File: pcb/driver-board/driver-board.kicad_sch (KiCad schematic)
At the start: 24 parts, among them Q3 IRLML6344, Q4 IRLML6344, Q5 IRLML6344

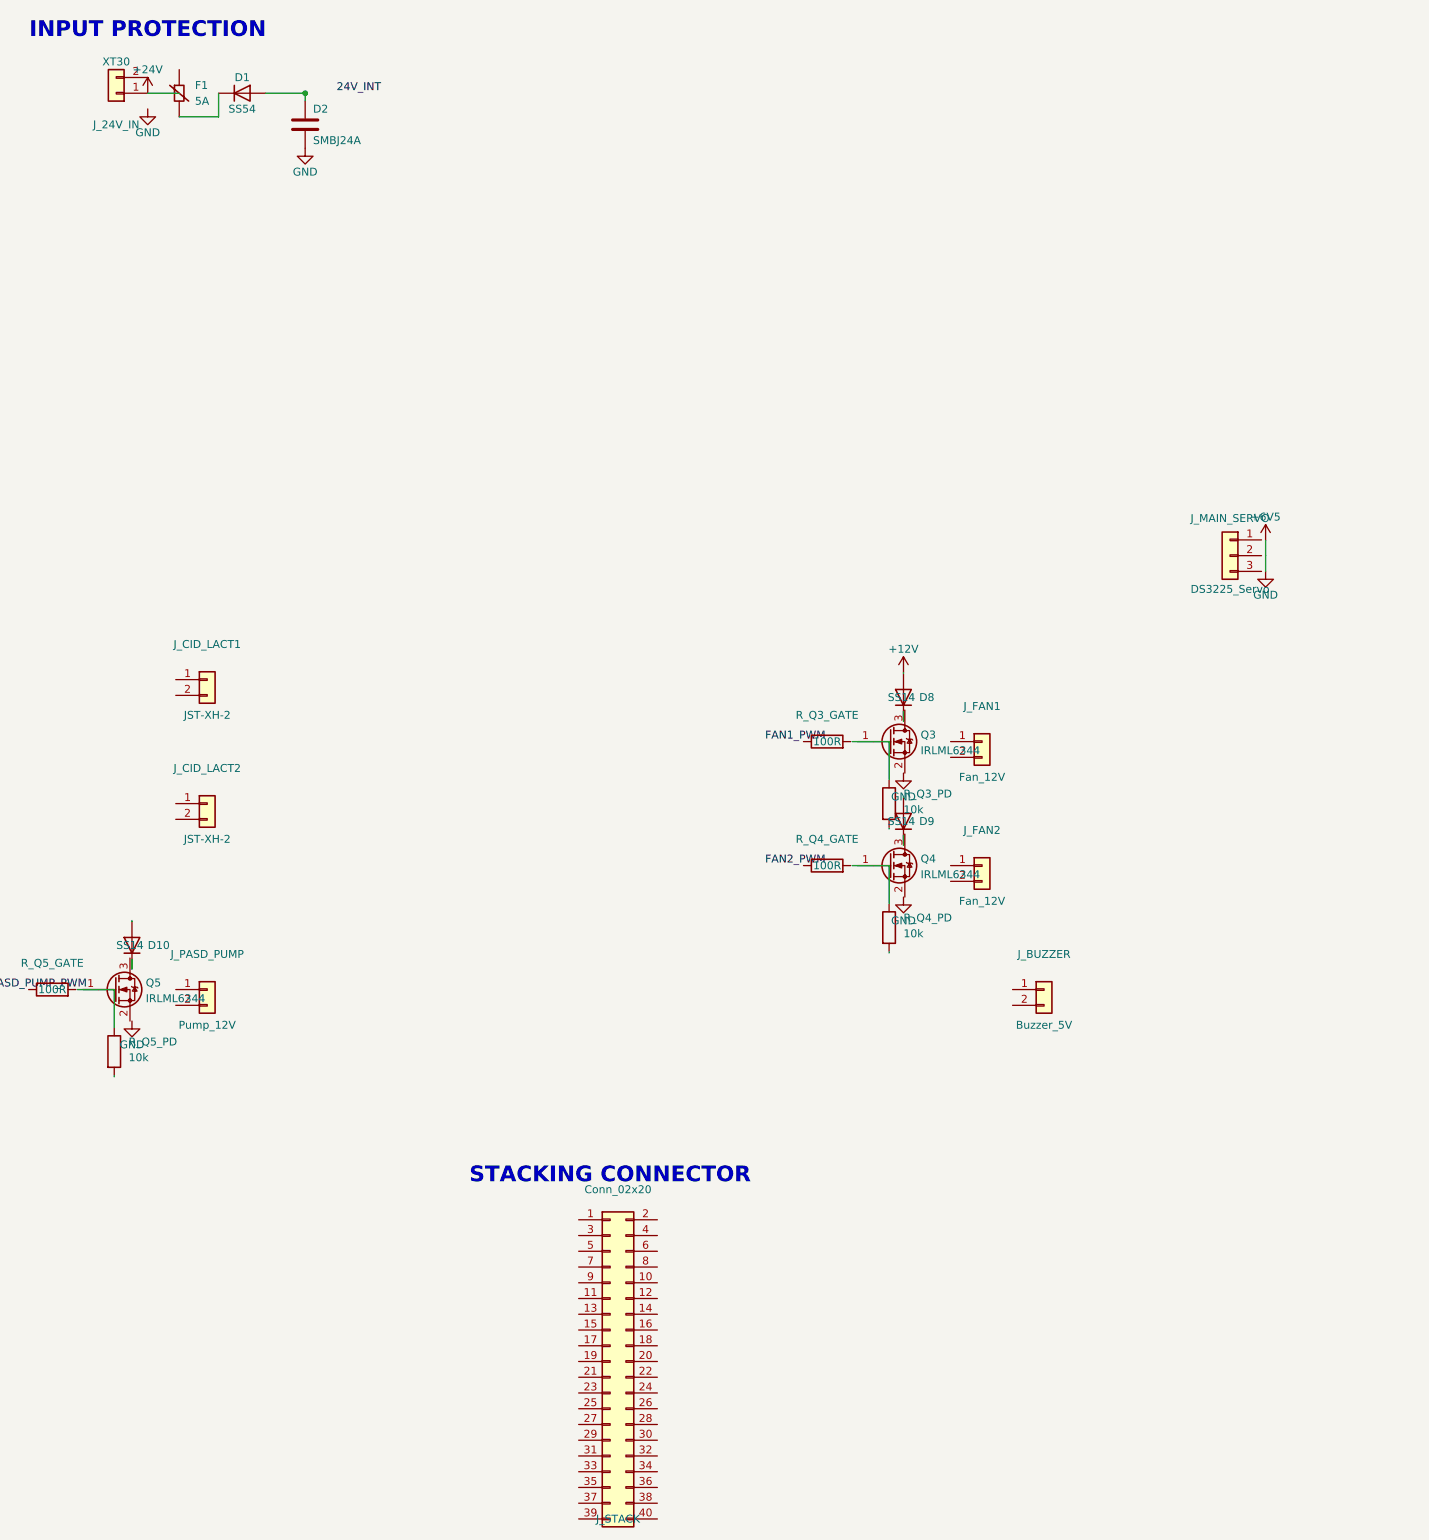
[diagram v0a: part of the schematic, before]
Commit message: Add driver board KiCAD PCB files, update to KiCAD 9, CM5IO off-the-shelf
- Create driver-board KiCAD 9 project: schematic, PCB layout, lib tables
- Update all PCB files from KiCAD 8 to KiCAD 9.0 (generator version,
  KICAD8_*_DIR → KICAD9_*_DIR env vars)
- Fix controller schematic parenthesis syntax error (pin 27/28)
- Update CM5IO Board status to off-the-shelf across all docs
  (was "Custom design required")
- Update docs: Repository Plan, Architecture, Components, Resource
  Allocation, PCB epic

Co-Authored-By: Claude Opus 4.6 <noreply@anthropic.com>
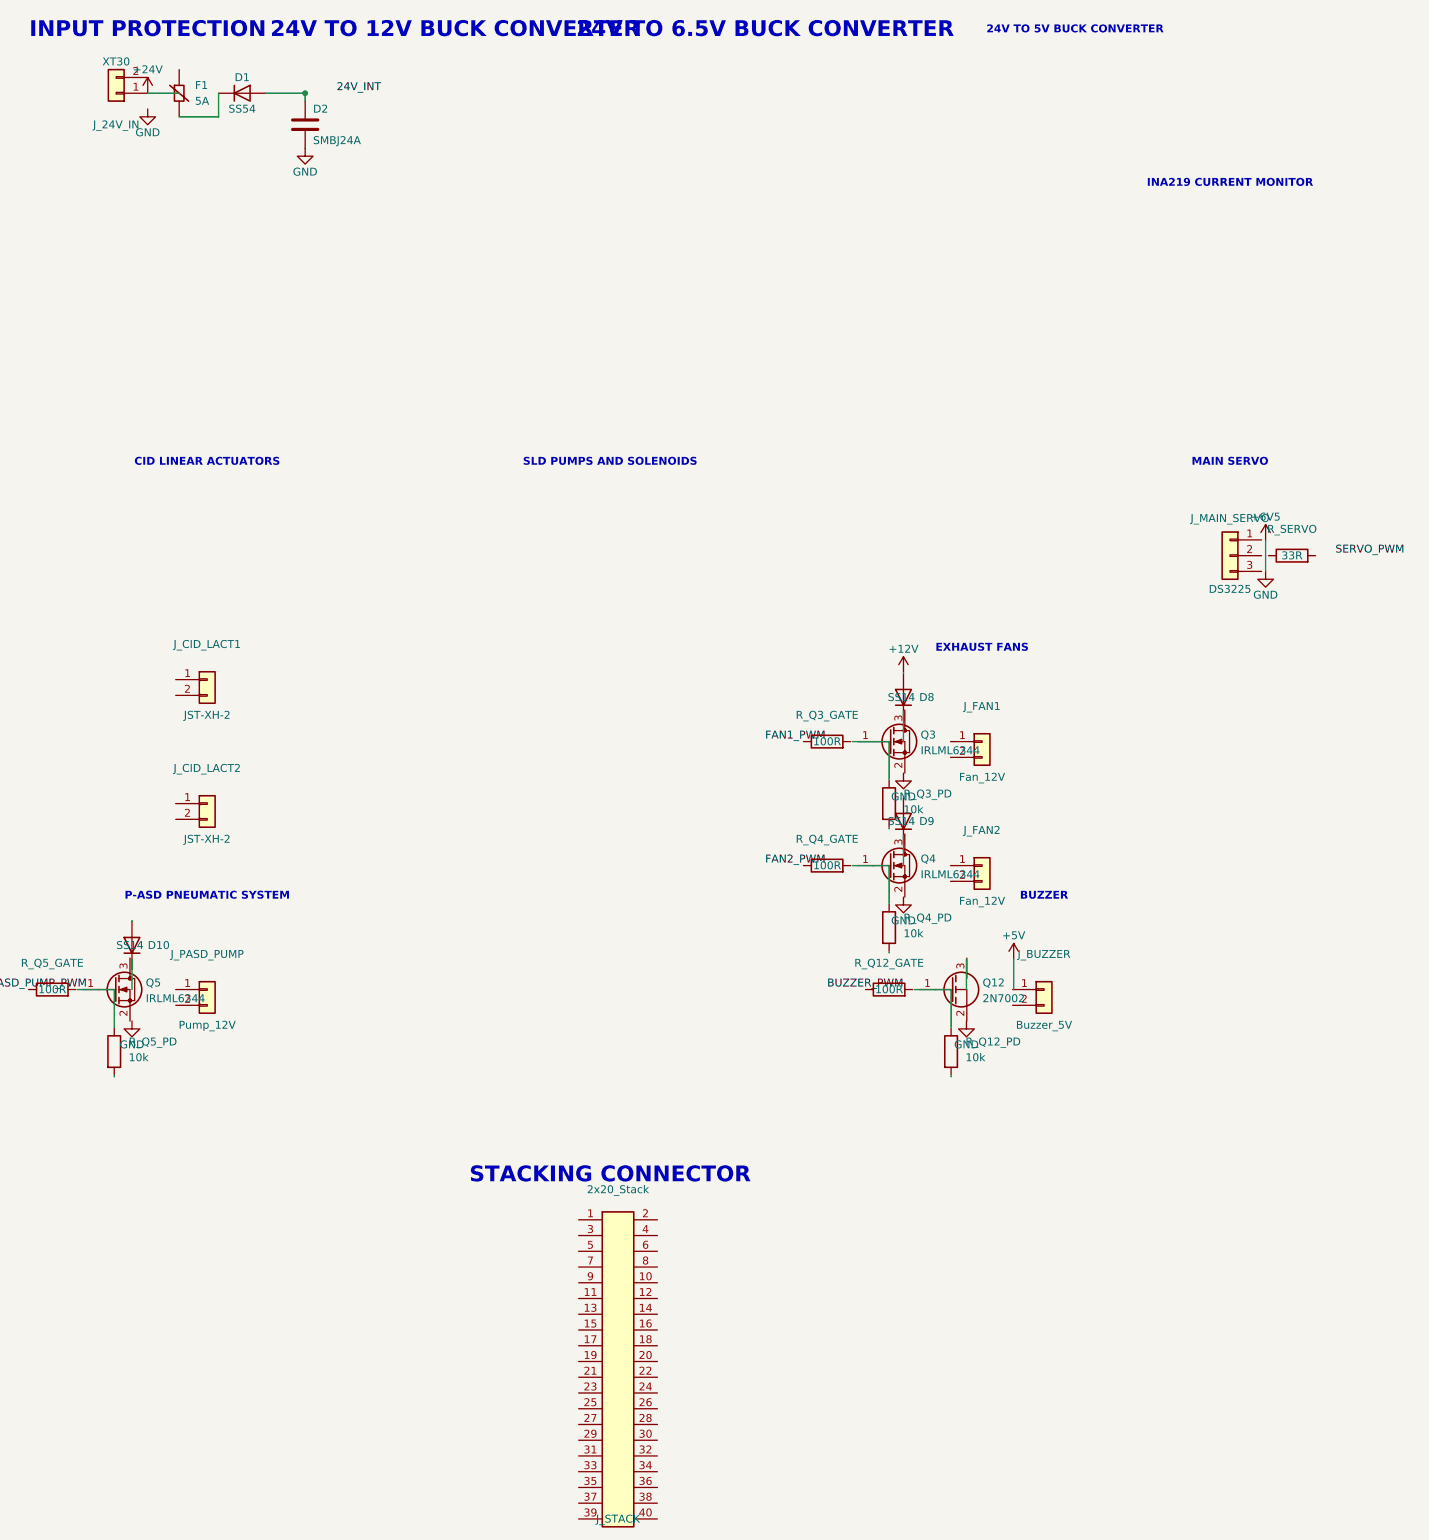
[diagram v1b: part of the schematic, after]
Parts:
- added Q12: 2N7002, Package_TO_SOT_SMD:SOT-23, symbol Transistor_FET:2N7002
- added R_Q12_GATE: 100R, Resistor_SMD:R_0603_1608Metric, symbol Device:R
- added R_Q12_PD: 10k, Resistor_SMD:R_0603_1608Metric, symbol Device:R
- added R_SERVO: 33R, Resistor_SMD:R_0603_1608Metric, symbol Device:R
- J_MAIN_SERVO: value DS3225_Servo -> DS3225
- J_STACK: value Conn_02x20 -> 2x20_Stack
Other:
- note added: "24V TO 12V BUCK CONVERTER"
- note added: "24V TO 5V BUCK CONVERTER"
- note added: "24V TO 6.5V BUCK CONVERTER"
- note added: "BUZZER"
- note added: "CID LINEAR ACTUATORS"
- note added: "EXHAUST FANS"
- note added: "INA219 CURRENT MONITOR"
- note added: "MAIN SERVO"
- note added: "P-ASD PNEUMATIC SYSTEM"
- note added: "SLD PUMPS AND SOLENOIDS"

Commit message: Fix driver board KiCad file syntax errors and update design files
Fix S-expression parsing errors: remove extra generator arg, convert bare
bold keyword to (bold yes), remove invalid (justify center) clauses.

Co-Authored-By: Claude Opus 4.6 <noreply@anthropic.com>
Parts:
- added C_BULK1: 470uF/10V, Capacitor_THT:CP_Radial_D8.0mm_P3.50mm, symbol Device:C_Polarized
- added C_BULK3: 100uF/25V, Capacitor_THT:CP_Radial_D6.3mm_P2.50mm, symbol Device:C_Polarized
- added C_BULK5V: 220uF/10V, Capacitor_THT:CP_Radial_D6.3mm_P2.50mm, symbol Device:C_Polarized
- added C_IN1, C_IN2, C_IN3: 10uF, Capacitor_SMD:C_0805_2012Metric, symbol Device:C
- added C_OUT1a, C_OUT1b, C_OUT2a, C_OUT2b, C_OUT3a, C_OUT3b: 22uF, Capacitor_SMD:C_0805_2012Metric, symbol Device:C
- added C_VCC6, C_VDD8, C_VM4, C_VM5, C_VM6, C_VS7: 100nF, Capacitor_SMD:C_0402_1005Metric, symbol Device:C
- added D11, D12, D13, D14, D15, D16, D6, D7: SS14, Diode_SMD:D_SMA, symbol Diode:SS54
- added D3: SMBJ12A, Diode_SMD:D_SMB, symbol Device:C
- added D4: SMBJ6.5A, Diode_SMD:D_SMB, symbol Device:C
- added D5: SMBJ5.0A, Diode_SMD:D_SMB, symbol Device:C
- added D_BST1, D_BST2, D_BST3: SS34, Diode_SMD:D_SMA, symbol Diode:SS54
- added F2: 1.5A, Resistor_SMD:R_0805_2012Metric, symbol Device:Polyfuse
- added F3: 3A, Resistor_SMD:R_1206_3216Metric, symbol Device:Polyfuse
- added F4: 2A, Resistor_SMD:R_1206_3216Metric, symbol Device:Polyfuse
- added J_PASD_SOL1: PASD_SOL1, Connector_JST:JST_XH_B2B-XH-A_1x02_P2.50mm_Vertical, symbol Connector_Generic:Conn_01x02
- added J_PASD_SOL2: PASD_SOL2, Connector_JST:JST_XH_B2B-XH-A_1x02_P2.50mm_Vertical, symbol Connector_Generic:Conn_01x02
- added J_PASD_SOL3: PASD_SOL3, Connector_JST:JST_XH_B2B-XH-A_1x02_P2.50mm_Vertical, symbol Connector_Generic:Conn_01x02
- added J_PASD_SOL4: PASD_SOL4, Connector_JST:JST_XH_B2B-XH-A_1x02_P2.50mm_Vertical, symbol Connector_Generic:Conn_01x02
- added J_PASD_SOL5: PASD_SOL5, Connector_JST:JST_XH_B2B-XH-A_1x02_P2.50mm_Vertical, symbol Connector_Generic:Conn_01x02
- added J_PASD_SOL6: PASD_SOL6, Connector_JST:JST_XH_B2B-XH-A_1x02_P2.50mm_Vertical, symbol Connector_Generic:Conn_01x02
- added J_SLD: SLD, Connector_JST:JST_XH_B8B-XH-A_1x08_P2.50mm_Vertical, symbol Connector_Generic:Conn_01x08
- added J_SLD_SOL1: SLD_SOL1, Connector_JST:JST_XH_B2B-XH-A_1x02_P2.50mm_Vertical, symbol Connector_Generic:Conn_01x02
- added J_SLD_SOL2: SLD_SOL2, Connector_JST:JST_XH_B2B-XH-A_1x02_P2.50mm_Vertical, symbol Connector_Generic:Conn_01x02
- added L1: 33uH, Inductor_SMD:L_1210_3225Metric, symbol Device:L
- added L2, L3: 22uH, Inductor_SMD:L_1210_3225Metric, symbol Device:L
- added Q1, Q10, Q11, Q2, Q6, Q7, Q8, Q9: IRLML6344, Package_TO_SOT_SMD:SOT-23, symbol Transistor_FET:IRLML6344
- added R_FB1_BOT, R_FB2_BOT, R_FB3_BOT, R_Q10_PD, R_Q11_PD, R_Q1_PD, R_Q2_PD, R_Q6_PD, R_Q7_PD, R_Q8_PD, R_Q9_PD: 10k, Resistor_SMD:R_0402_1005Metric, symbol Device:R
- added R_FB1_TOP: 140k, Resistor_SMD:R_0402_1005Metric, symbol Device:R
- added R_FB2_TOP: 71.5k, Resistor_SMD:R_0402_1005Metric, symbol Device:R
- added R_FB3_TOP: 52.3k, Resistor_SMD:R_0402_1005Metric, symbol Device:R
- added R_Q10_GATE, R_Q11_GATE, R_Q1_GATE, R_Q2_GATE, R_Q6_GATE, R_Q7_GATE, R_Q8_GATE, R_Q9_GATE: 100R, Resistor_SMD:R_0402_1005Metric, symbol Device:R
- added R_SENSE1, R_SENSE2: 1k, Resistor_SMD:R_0402_1005Metric, symbol Device:R
- added R_SHUNT: 10mR, Resistor_SMD:R_2512_6332Metric, symbol Device:R
- added U1: MP1584EN_12V, Package_TO_SOT_SMD:SOT-23-8, symbol Driver:MP1584EN
- added U2: MP1584EN_6V5, Package_TO_SOT_SMD:SOT-23-8, symbol Driver:MP1584EN
- added U3: MP1584EN_5V, Package_TO_SOT_SMD:SOT-23-8, symbol Driver:MP1584EN
- added U4, U5: DRV8876, Package_SO:WSON-8-1EP_2x2mm_P0.5mm_EP0.9x1.6mm, symbol Driver:DRV8876
- added U6: TB6612FNG, Package_SO:SSOP-24_3.9x8.7mm_P0.635mm, symbol Driver:TB6612FNG
- added U7: INA219, Package_TO_SOT_SMD:SOT-23-8, symbol Driver:INA219
- added U8: PCF8574, Package_SO:SOIC-16_3.9x9.9mm_P1.27mm, symbol Driver:PCF8574
- J_BUZZER: value Buzzer_5V -> Buzzer
- J_CID_LACT1: value JST-XH-2 -> CID_LACT1
- J_CID_LACT2: value JST-XH-2 -> CID_LACT2
- J_FAN1: value Fan_12V -> Fan1
- J_FAN2: value Fan_12V -> Fan2
- J_PASD_PUMP: value Pump_12V -> PASD_Pump
- J_STACK: value 2x20_Stack -> J_STACK
- R_Q12_GATE, R_Q12_PD, R_Q3_GATE, R_Q3_PD, R_Q4_GATE, R_Q4_PD, R_Q5_GATE, R_Q5_PD, R_SERVO: footprint Resistor_SMD:R_0603_1608Metric -> Resistor_SMD:R_0402_1005Metric
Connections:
- net BUZZER_PWM: now also J_STACK.38 (Pin_38), R_Q12_GATE.1
- net FAN1_PWM: now also J_STACK.27 (Pin_27), Q3.1 (G), R_Q3_GATE.1
- net FAN2_PWM: now also J_STACK.28 (Pin_28), Q4.1 (G), R_Q4_GATE.1
- net PASD_PUMP_PWM: now also J_STACK.15 (Pin_15), Q5.1 (G), R_Q5_GATE.1
- net CID_LACT1_EN: now reaches J_STACK.21 (Pin_21)
- net CID_LACT1_PH: now reaches J_STACK.22 (Pin_22)
- net CID_LACT1_PH: now also U4.7 (PH)
- net CID_LACT2_EN: now reaches J_STACK.23 (Pin_23)
- net CID_LACT2_PH: now reaches J_STACK.24 (Pin_24)
- net CID_LACT2_PH: now also U5.7 (PH)
- net SLD_PUMP1_PWM: now reaches J_STACK.29 (Pin_29)
- net SLD_PUMP1_DIR: now reaches J_STACK.30 (Pin_30)
- net SLD_PUMP2_PWM: now reaches J_STACK.31 (Pin_31)
- net SLD_PUMP2_DIR: now reaches J_STACK.32 (Pin_32)
- net SLD_PUMP2_DIR: now also U6.18 (BIN1)
- net SLD_SOL1_EN: now reaches J_STACK.33 (Pin_33)
- net SLD_SOL1_EN: now also Q1.1 (G), R_Q1_GATE.1
- net SLD_SOL2_EN: now reaches J_STACK.34 (Pin_34)
- net SLD_SOL2_EN: now also Q2.1 (G), R_Q2_GATE.1
- net I2C1_SCL: now reaches J_STACK.35 (Pin_35)
- net I2C1_SCL: now also U8.14 (SCL)
- net I2C1_SDA: now reaches J_STACK.36 (Pin_36)
- net MAIN_SERVO_PWM: now reaches J_STACK.37 (Pin_37)
- net +24V: no longer names the net of J_24V_IN.1 (Pin_1)
- net +6V5: no longer names the net of D2.2
- new net PCF_P0: Q6.1 (G), R_Q6_GATE.1, U8.4 (P0)
- new net PCF_P1: Q7.1 (G), R_Q7_GATE.1, U8.5 (P1)
- new net PCF_P2: Q8.1 (G), R_Q8_GATE.1, U8.6 (P2)
- new net PCF_P3: Q9.1 (G), R_Q9_GATE.1, U8.7 (P3)
- new net PCF_P4: Q10.1 (G), R_Q10_GATE.1, U8.9 (P4)
- new net PCF_P5: Q11.1 (G), R_Q11_GATE.1, U8.10 (P5)
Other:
- note removed: "24V TO 12V BUCK CONVERTER"
- note removed: "24V TO 5V BUCK CONVERTER"
- note removed: "24V TO 6.5V BUCK CONVERTER"
- note removed: "BUZZER"
- note removed: "CID LINEAR ACTUATORS"
- note removed: "EXHAUST FANS"
- note removed: "INA219 CURRENT MONITOR"
- note removed: "INPUT PROTECTION"
- note removed: "MAIN SERVO"
- note removed: "P-ASD PNEUMATIC SYSTEM"
- note removed: "SLD PUMPS AND SOLENOIDS"
- note removed: "STACKING CONNECTOR"
